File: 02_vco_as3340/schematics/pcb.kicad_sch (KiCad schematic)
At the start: 75 parts, among them Q1 BC547C, Q2 BC547C, U1 TL072, U2 AS3340, U3 TL074

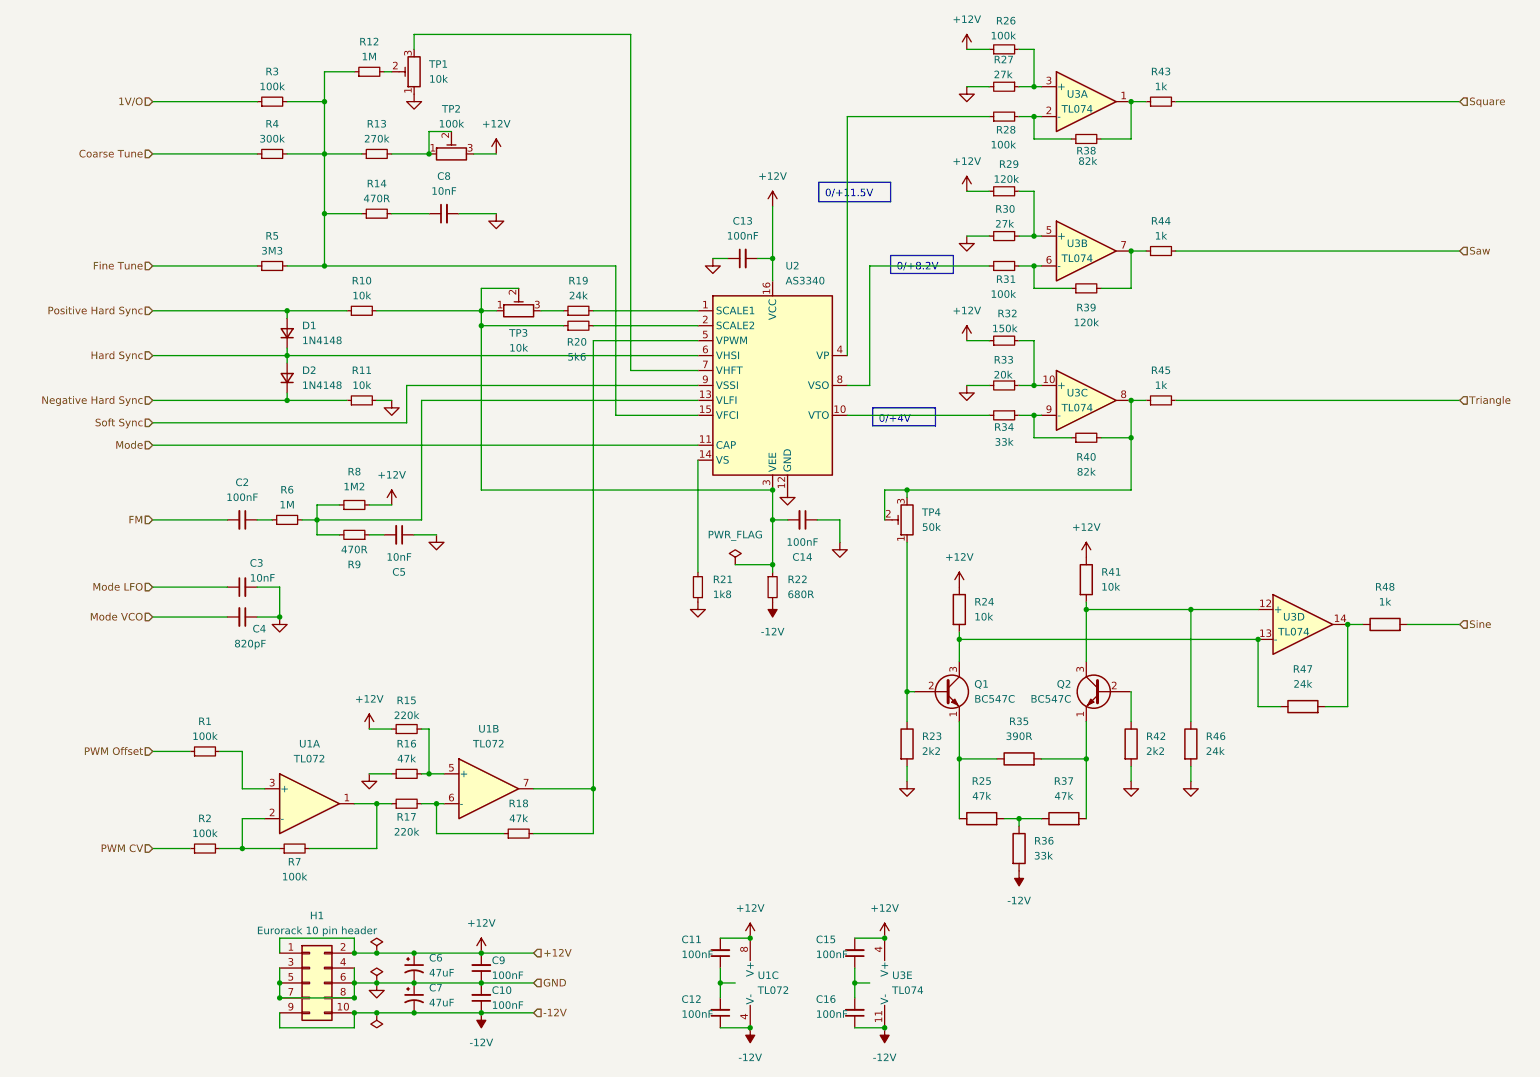
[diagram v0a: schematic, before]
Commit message: updated PCBs for 02 and 03
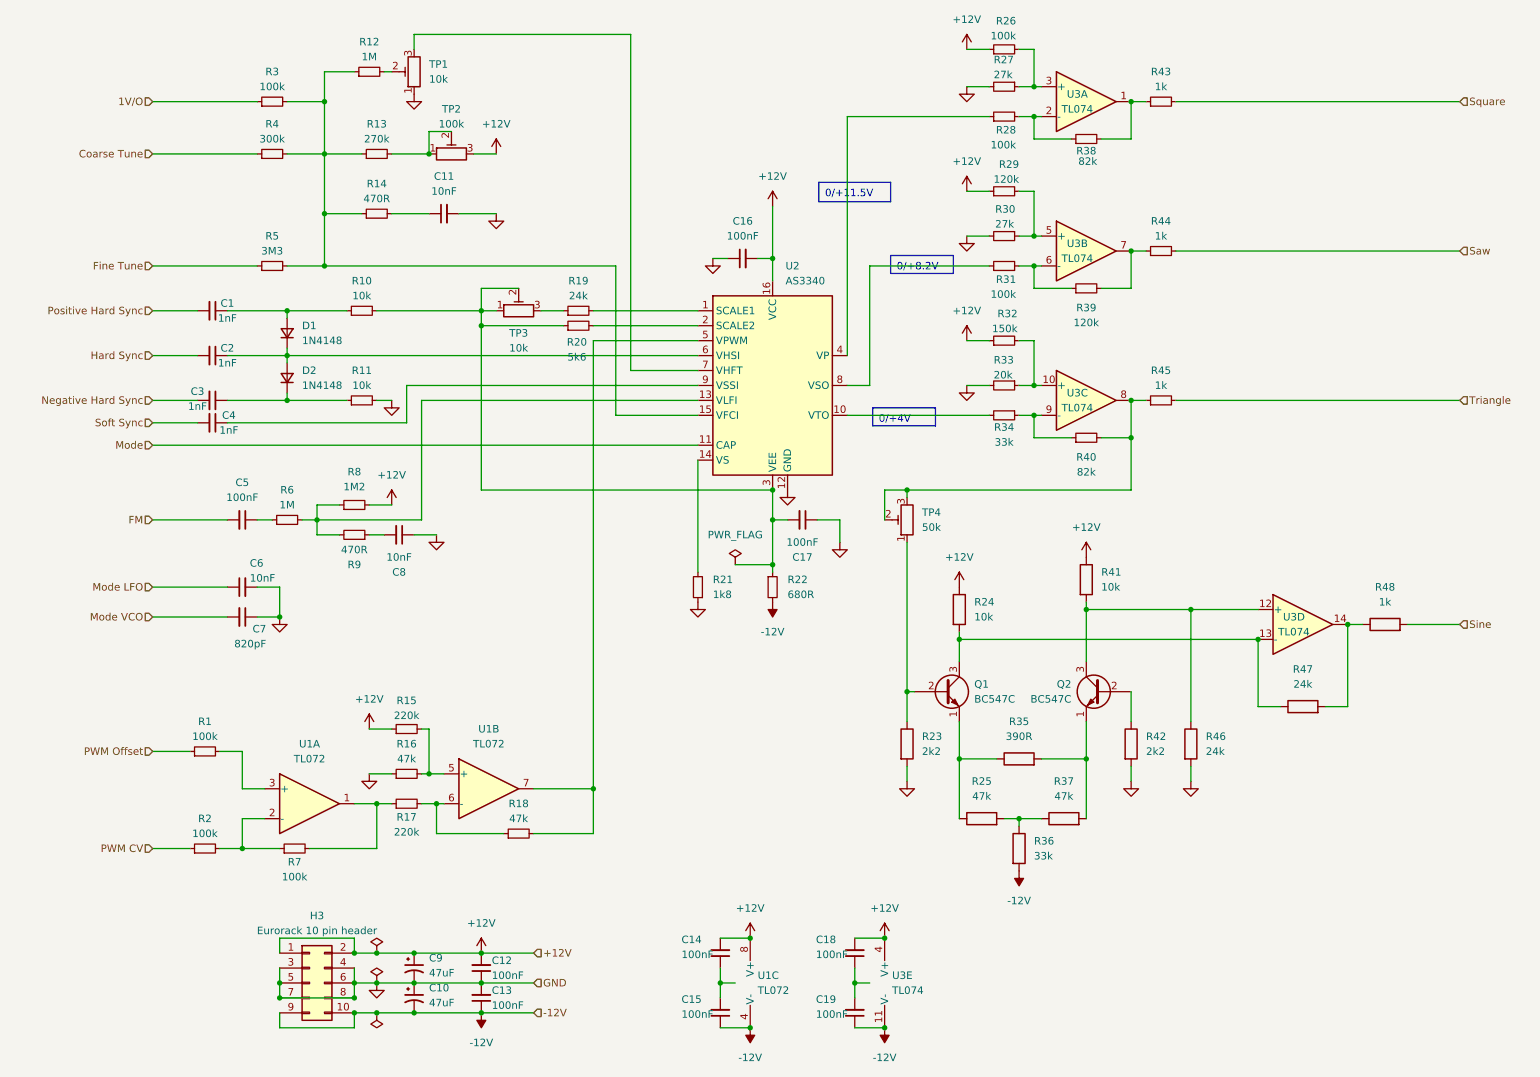
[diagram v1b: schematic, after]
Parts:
- added C1, C2, C3, C4: 1nF, Capacitor_THT:C_Disc_D6.0mm_W2.5mm_P5.00mm, symbol Device:C_Small
- renumbered C7 to C10, C8 to C11, C9 to C12, C10 to C13, C11 to C14, C12 to C15, C13 to C16, C14 to C17, C15 to C18, C16 to C19, C2 to C5, C3 to C6, C4 to C7, C5 to C8, C6 to C9, H1 to H3
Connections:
- net Hard Sync: now also C2.2; no longer D1.1 (K), D2.2 (A), U2.6 (VHSI)
- net Negative Hard Sync: now also C3.2; no longer D2.1 (K), R11.1
- net Positive Hard Sync: now also C1.2; no longer D1.2 (A), R10.1
- net Soft Sync: now also C4.2; no longer U2.9 (VSSI)
- new net: C2.1, D1.1 (K), D2.2 (A), U2.6 (VHSI)
- new net: C1.1, D1.2 (A), R10.1
- new net: C3.1, D2.1 (K), R11.1
- new net: C4.1, U2.9 (VSSI)
